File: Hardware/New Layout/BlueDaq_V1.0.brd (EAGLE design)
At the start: 70.5 x 81 mm, 72 parts, among them IC1 MEGA8-AI, Q1 MMBT2222, Q2 MMBT2222, Q3 MMBT2222, Q4 MMBT2222, U1 MCP73831, U2 TPS61200, U3 BME280, U4 MIC5225-3.3, U5 MIC5219 5V, X1 USB-MICROB, X2 3.5mm, X4 3.5mm, Y1 16 mhz

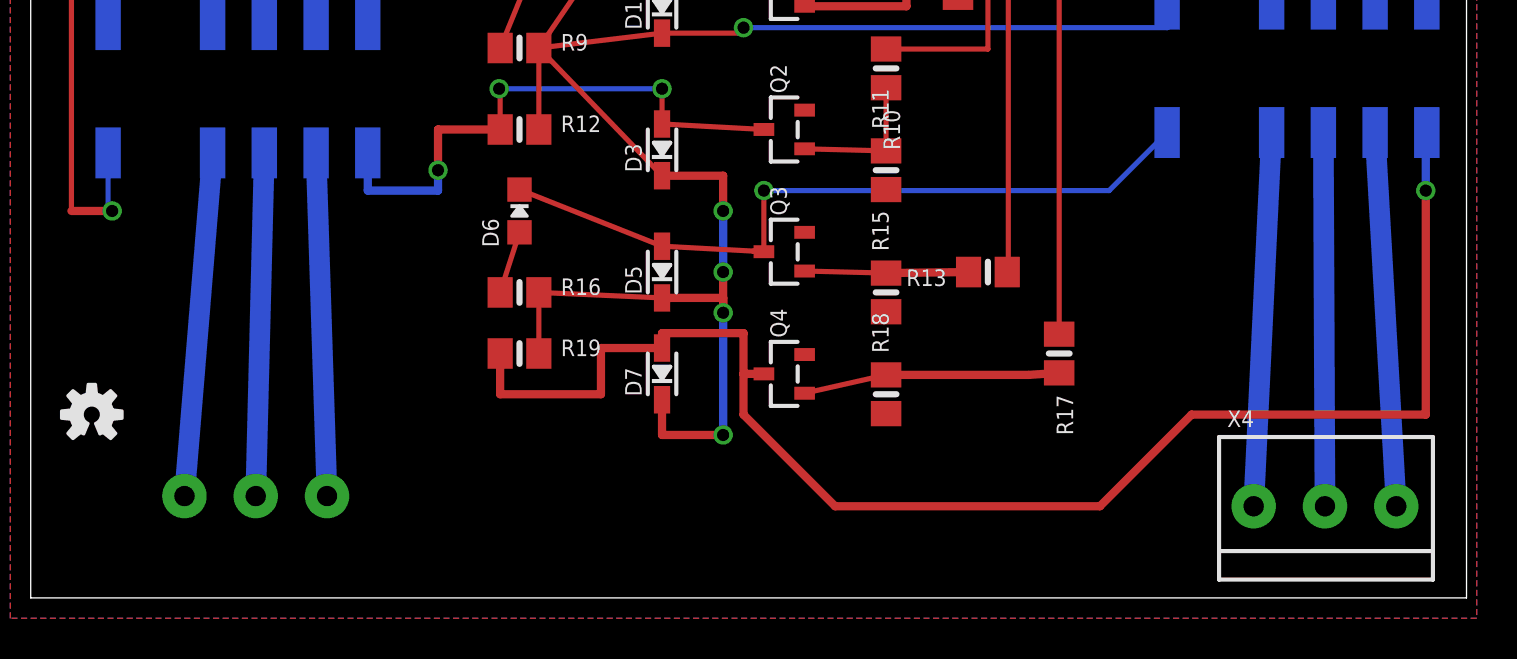
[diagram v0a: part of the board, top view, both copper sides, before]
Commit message: fixed relay, made board smaller
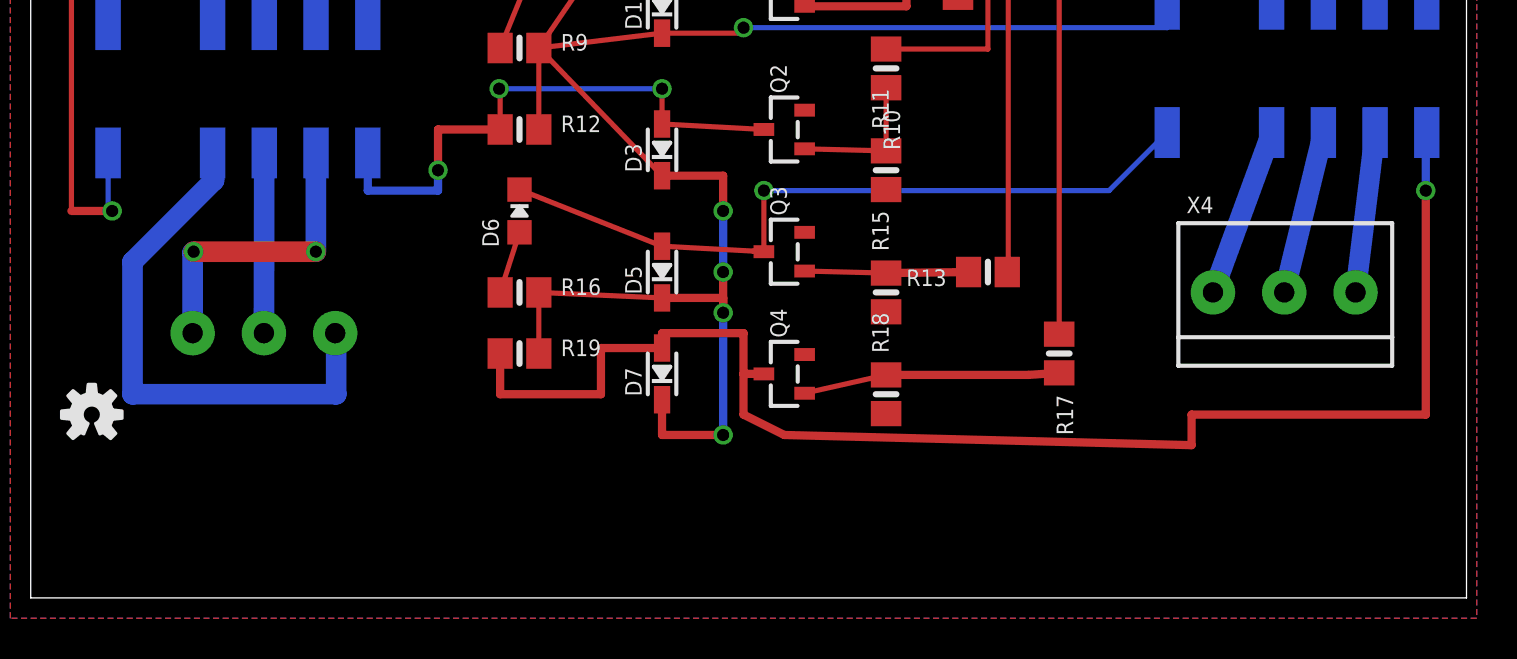
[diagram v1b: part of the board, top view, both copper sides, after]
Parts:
- moved X4 10.7 mm to (61.5, 15.0)
- moved X2 8.02 mm to (11.5, 13.0), turned to 0 degrees
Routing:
- net NO2: track 18.4 -> 7.91 mm
- net COM2: track 18.4 -> 8.08 mm
- net N$10: track 18.4 -> 8.36 mm
- net N$28: track 16.9 -> 26.6 mm
- net COM1: track 16.9 -> 8.85 mm
- net N$12: track 73.1 -> 71.1 mm
- net NO1: track 16.9 -> 14.9 mm, vias 0 -> 2
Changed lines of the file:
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@@
 </element>
 <element name="X1" library="SparkFun" package="USB-MICROB" value="USB-MICROB" x="67" y="71" rot="MR270"/>
-<element name="X2" library="microbuilder" package="TERMBLOCK_1X3-3.5MM" value="3.5mm" x="11" y="5" rot="MR180"/>
-<element name="X4" library="microbuilder" package="TERMBLOCK_1X3-3.5MM" value="3.5mm" x="63.5" y="4.5"/>
+<element name="X2" library="microbuilder" package="TERMBLOCK_1X3-3.5MM" value="3.5mm" x="11.5" y="13" rot="MR0"/>
+<element name="X4" library="microbuilder" package="TERMBLOCK_1X3-3.5MM" value="3.5mm" x="61.5" y="15"/>
 <element name="Y1" library="SparkFun-FreqCtrl" package="HC49U-V" value="16 mhz" x="66" y="52" rot="R270"/>
 <element name="C14" library="microbuilder" package="0805-NO@1" value="0.1uF" x="24" y="37" rot="R90"/>
@@
 <contactref element="X2" pad="2"/>
 <contactref element="RELAY_0" pad="9"/>
-<wire x1="11.05" y1="5" x2="11.47" y2="21.85" width="1.016" layer="16"/>
+<wire x1="11.45" y1="13" x2="11.47" y2="21.85" width="1.016" layer="16"/>
 </signal>
 <signal name="NO1" class="1">
 <contactref element="X2" pad="1"/>
 <contactref element="RELAY_0" pad="8"/>
-<wire x1="14.55" y1="5" x2="14.01" y2="21.85" width="1.016" layer="16"/>
+<wire x1="14.01" y1="21.85" x2="14" y2="21.84" width="1.016" layer="16"/>
+<wire x1="14" y1="21.84" x2="14" y2="17" width="1.016" layer="16"/>
+<wire x1="7.95" y1="13" x2="7.95" y2="16.95" width="1.016" layer="16"/>
+<wire x1="7.95" y1="16.95" x2="8" y2="17" width="1.016" layer="16"/>
+<via x="8" y="17" extent="1-16" drill="0.6" shape="square"/>
+<wire x1="8" y1="17" x2="14" y2="17" width="1.016" layer="1"/>
+<via x="14" y="17" extent="1-16" drill="0.6" shape="square"/>
 </signal>
 <signal name="N$26">
@@
 <contactref element="X2" pad="3"/>
 <contactref element="RELAY_0" pad="10"/>
-<wire x1="7.55" y1="5" x2="8.93" y2="21.85" width="1.016" layer="16"/>
+<wire x1="14.95" y1="13" x2="15" y2="13" width="1.016" layer="16"/>
+<wire x1="15" y1="13" x2="15" y2="10" width="1.016" layer="16"/>
+<wire x1="15" y1="10" x2="5" y2="10" width="1.016" layer="16"/>
+<wire x1="5" y1="10" x2="5" y2="16.5" width="1.016" layer="16"/>
+<wire x1="5" y1="16.5" x2="9" y2="20.5" width="1.016" layer="16"/>
+<wire x1="9" y1="20.5" x2="9" y2="21.78" width="1.016" layer="16"/>
+<wire x1="9" y1="21.78" x2="8.93" y2="21.85" width="1.016" layer="16"/>
 </signal>
 <signal name="N$25">
@@
 <contactref element="X4" pad="2"/>
 <contactref element="RELAY_1" pad="9"/>
-<wire x1="63.55" y1="4.5" x2="63.47" y2="22.85" width="1.016" layer="16"/>
+<wire x1="61.55" y1="15" x2="63.47" y2="22.85" width="1.016" layer="16"/>
 </signal>
 <signal name="NO2" class="1">
 <contactref element="X4" pad="1"/>
 <contactref element="RELAY_1" pad="8"/>
-<wire x1="67.05" y1="4.5" x2="66.01" y2="22.85" width="1.016" layer="16"/>
+<wire x1="65.05" y1="15" x2="66.01" y2="22.85" width="1.016" layer="16"/>
 </signal>
 <signal name="N$9">
@@
 <contactref element="X4" pad="3"/>
 <contactref element="RELAY_1" pad="10"/>
-<wire x1="60.05" y1="4.5" x2="60.93" y2="22.85" width="1.016" layer="16"/>
+<wire x1="58.05" y1="15" x2="60.93" y2="22.85" width="1.016" layer="16"/>
 </signal>
 <signal name="N$12">
@@
 <wire x1="68.5" y1="20" x2="68.5" y2="9" width="0.4064" layer="1"/>
 <wire x1="68.5" y1="9" x2="57" y2="9" width="0.4064" layer="1"/>
-<wire x1="57" y1="9" x2="52.5" y2="4.5" width="0.4064" layer="1"/>
-<wire x1="52.5" y1="4.5" x2="39.5" y2="4.5" width="0.4064" layer="1"/>
-<wire x1="39.5" y1="4.5" x2="35" y2="9" width="0.4064" layer="1"/>
+<wire x1="57" y1="9" x2="57" y2="7.5" width="0.4064" layer="1"/>
+<wire x1="57" y1="7.5" x2="37" y2="8" width="0.4064" layer="1"/>
+<wire x1="37" y1="8" x2="35" y2="9" width="0.4064" layer="1"/>
 <wire x1="35" y1="9" x2="35" y2="11" width="0.4064" layer="1"/>
 </signal>

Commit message: more small fixes
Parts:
- moved JP1 5.66 mm to (10.2, 46.1), turned to 180 degrees
- moved X1 2.00 mm to (69.0, 71.0)
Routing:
- net VBATT: track 112.6 -> 104.6 mm
- net N$23: track 68.1 -> 69.9 mm
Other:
- board size 70.5 x 81 mm -> 70.5 x 75 mm
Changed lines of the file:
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@@
 <board>
 <plain>
-<wire x1="0" y1="0" x2="70.5" y2="0" width="0" layer="20"/>
-<wire x1="70.5" y1="0" x2="70.5" y2="81" width="0" layer="20"/>
+<wire x1="0" y1="6" x2="70.5" y2="6" width="0" layer="20"/>
+<wire x1="70.5" y1="6" x2="70.5" y2="81" width="0" layer="20"/>
 <wire x1="70.5" y1="81" x2="0" y2="81" width="0" layer="20"/>
-<wire x1="0" y1="81" x2="0" y2="0" width="0" layer="20"/>
+<wire x1="0" y1="81" x2="0" y2="6" width="0" layer="20"/>
 </plain>
 <attributes>
@@
 <attribute name="OC_FARNELL" value="9171371" x="48" y="53" size="1.778" layer="27" rot="R180" display="off"/>
 </element>
-<element name="JP1" library="SparkFun" package="JST-2-SMD" value="LiPo" x="6.37" y="50.25" rot="MR90"/>
+<element name="JP1" library="SparkFun" package="JST-2-SMD" value="LiPo" x="10.25" y="46.13" rot="MR180"/>
 <element name="JTAG" library="pinhead" package="2X03" value="" x="32" y="53" rot="R270"/>
 <element name="L1" library="SparkFun" package="CDRH2D09" value="4.7uH, 1.2A" x="37" y="61.5"/>
@@
 <attribute name="PROD_ID" value="VREG-10107" x="24" y="67" size="1.778" layer="27" display="off"/>
 </element>
-<element name="X1" library="SparkFun" package="USB-MICROB" value="USB-MICROB" x="67" y="71" rot="MR270"/>
+<element name="X1" library="SparkFun" package="USB-MICROB" value="USB-MICROB" x="69" y="71" rot="MR270"/>
 <element name="X2" library="microbuilder" package="TERMBLOCK_1X3-3.5MM" value="3.5mm" x="11.5" y="13" rot="MR0"/>
 <element name="X4" library="microbuilder" package="TERMBLOCK_1X3-3.5MM" value="3.5mm" x="61.5" y="15"/>
@@
 <wire x1="34" y1="76" x2="34.25" y2="76" width="0.254" layer="1"/>
 <wire x1="16.05" y1="59.5" x2="15.05" y2="65" width="0.4064" layer="1"/>
-<wire x1="16.05" y1="59.5" x2="16.05" y2="57.5" width="0.254" layer="1"/>
-<wire x1="16.05" y1="57.5" x2="33" y2="57.5" width="0.254" layer="1"/>
+<wire x1="16.05" y1="59.5" x2="16.05" y2="57.5" width="0.4064" layer="1"/>
+<wire x1="16.05" y1="57.5" x2="33" y2="57.5" width="0.4064" layer="1"/>
 <wire x1="53.5" y1="54" x2="54" y2="53.5" width="0.254" layer="1"/>
 <wire x1="54" y1="53.5" x2="54" y2="53" width="0.254" layer="1"/>
@@
 <via x="16.5" y="73.5" extent="1-16" drill="0.6" shape="square"/>
 <wire x1="16.5" y1="73.5" x2="16.5" y2="76" width="0.254" layer="1"/>
-<wire x1="33" y1="57.5" x2="33.27" y2="55.54" width="0.254" layer="1"/>
+<wire x1="33" y1="57.5" x2="33.27" y2="55.54" width="0.4064" layer="1"/>
 <wire x1="35.5" y1="44" x2="35.5" y2="55.5" width="0.254" layer="16"/>
 <via x="35.5" y="55.5" extent="1-16" drill="0.6" shape="square"/>
@@
 <vertex x="-1" y="81"/>
 <vertex x="71" y="81"/>
-<vertex x="71" y="-1"/>
-<vertex x="-1" y="-1"/>
+<vertex x="70.5" y="6.5"/>
+<vertex x="-1.5" y="6.5"/>
 </polygon>
 <polygon width="0.4064" layer="16">
 <vertex x="-1" y="81"/>
 <vertex x="71" y="81"/>
-<vertex x="71" y="-1"/>
-<vertex x="-1" y="-1"/>
+<vertex x="70.5" y="6.5"/>
+<vertex x="-1.5" y="6.5"/>
 </polygon>
 <wire x1="38.5" y1="53.5" x2="39" y2="50.5" width="0.254" layer="1"/>
@@
 <wire x1="52.05" y1="67.5" x2="52.05" y2="69.35" width="0.4064" layer="1"/>
 <wire x1="52.05" y1="69.35" x2="52" y2="69.35" width="0.254" layer="1"/>
-<wire x1="2.67" y1="51.25" x2="13" y2="51.33" width="0.4064" layer="16"/>
+<wire x1="11.25" y1="49.83" x2="13" y2="51.33" width="0.4064" layer="16"/>
 <wire x1="13" y1="51.33" x2="13" y2="65" width="0.4064" layer="16"/>
 <wire x1="13" y1="65" x2="9.5" y2="65" width="0.4064" layer="16"/>
@@
 <wire x1="60.63" y1="75.93" x2="62" y2="74" width="0.4064" layer="1"/>
 <via x="62" y="74" extent="1-16" drill="0.6" shape="square"/>
-<wire x1="62" y1="74" x2="64.35" y2="72.3" width="0.4064" layer="16"/>
+<wire x1="62" y1="74" x2="66.35" y2="72.3" width="0.4064" layer="16"/>
 <wire x1="57.35" y1="72" x2="60.63" y2="75.93" width="0.4064" layer="1"/>
 <wire x1="11" y1="76" x2="11" y2="80" width="0.4064" layer="1"/>

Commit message: Board update
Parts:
- moved JP1 6.62 mm to (3.63, 46.2), turned to 270 degrees
- moved C4 6.00 mm to (43.0, 61.2)
- moved +9V 6.00 mm to (23.0, 54.0)
- moved -9V 6.00 mm to (27.0, 54.0)
- moved BT 6.00 mm to (2.00, 34.0)
- moved C1 6.00 mm to (66.0, 55.9)
- moved C10 6.00 mm to (52.0, 64.0)
- moved C11 6.00 mm to (17.5, 31.0)
- moved C12 6.00 mm to (29.0, 62.0)
- moved C13 6.00 mm to (17.0, 53.5)
- moved C14 6.00 mm to (24.0, 31.0)
- moved C2 6.00 mm to (66.0, 37.0)
- moved C3 6.00 mm to (56.7, 41.0)
- moved C5 6.00 mm to (32.0, 60.0)
- moved C6 6.00 mm to (32.5, 66.0)
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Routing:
- net BT_RX: track 20.5 -> 70.5 mm, vias 2 -> 4
- net VCC: track 164.3 -> 207.2 mm
- net BT_STS: track 37.8 -> 67.1 mm, vias 2 -> 4
- net BT_BRK: track 27.0 -> 56.2 mm, vias 0 -> 2
- net BT_TX: track 49.7 -> 66.9 mm
- net GND: track 12.9 -> 27.6 mm, vias 2 -> 4
- net PGND: track 13.5 -> 3.99 mm
- net VBATT: track 104.6 -> 108.4 mm
- net N$28: track 26.6 -> 27.7 mm
- net N$6: track 58.8 -> 58.1 mm
- net XTAL1: track 20.7 -> 21.3 mm
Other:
- board text added: "T05, 11/16/2016, Rev 2.0"

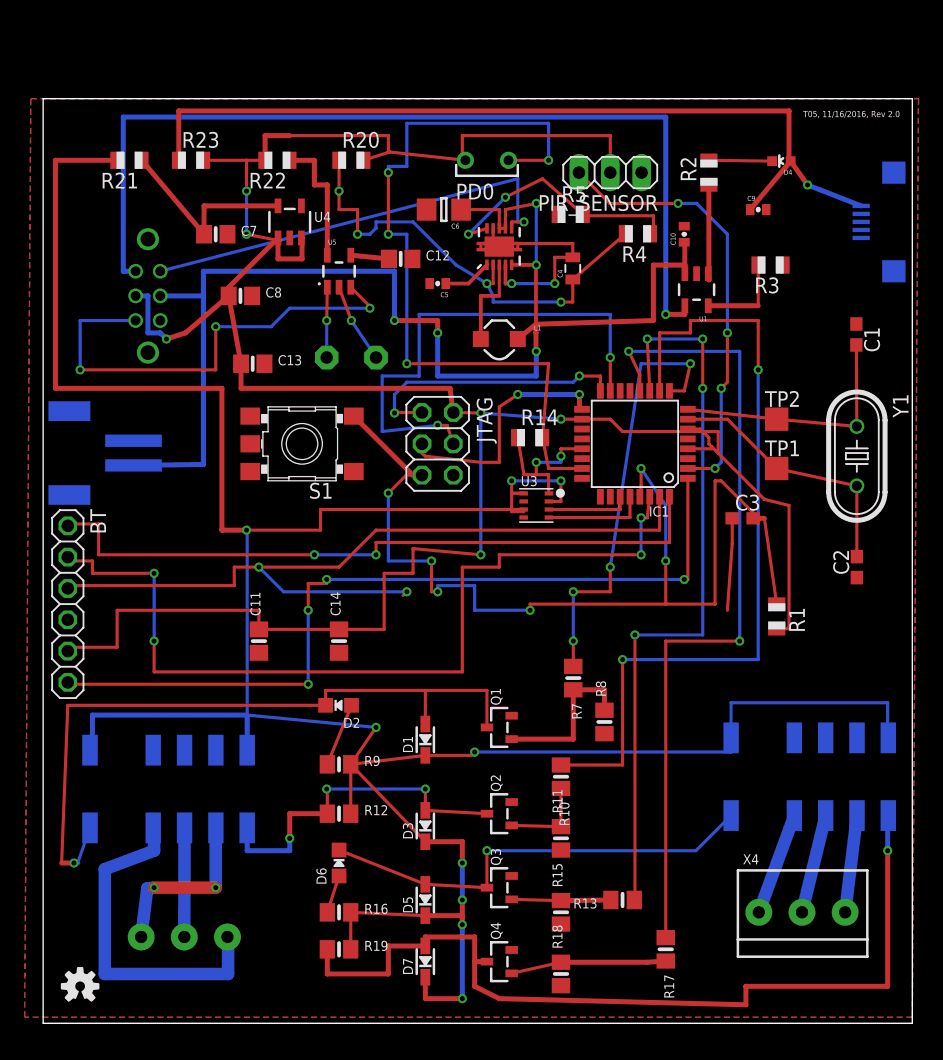
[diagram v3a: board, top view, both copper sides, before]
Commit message: trace size fixes
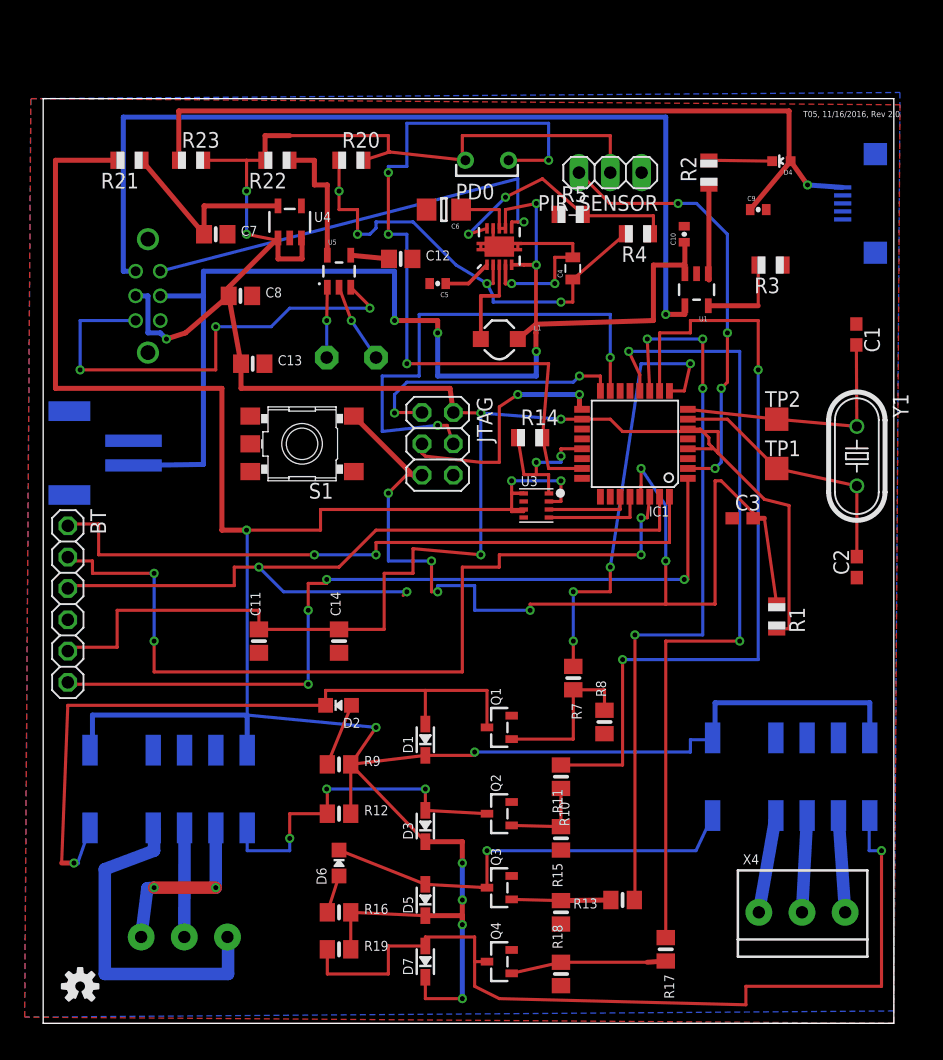
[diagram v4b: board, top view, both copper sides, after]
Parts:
- moved X1 2.12 mm to (67.5, 66.5)
- moved RELAY_1 1.50 mm to (60.5, 20.0)
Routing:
- net BT_DTR: track 7.47 -> 0.00 mm
- net N$23: track 69.9 -> 68.0 mm
- net 3.3V: track 231.3 -> 229.8 mm
- net N$7: track 36.5 -> 35.6 mm
- net N$12: track 71.1 -> 71.6 mm
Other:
- board size 70.5 x 75 mm -> 69 x 75 mm
